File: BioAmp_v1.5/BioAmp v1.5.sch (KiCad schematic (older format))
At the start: 27 parts, among them J1 Conn_01x02_Male, J2 PJ-3062-CO, J4 Conn_01x03_Male, J5 Conn_01x02_Male, J6 Conn_01x02_Male, J7 Conn_01x02_Male, U1 TL074

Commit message: update v1.5.4
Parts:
- removed C2: 100nf, Capacitor_THT:C_Disc_D3.8mm_W2.6mm_P2.50mm, symbol Device:C
- added C2, C8: CP, Capacitor_THT:CP_Radial_D5.0mm_P2.50mm, symbol Device:CP
- S1: footprint udlabs:TL2285EE -> udlabs:G64_DPDT
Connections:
- net ACout: now also C2.2; no longer J2.2 (TIP), J2.3 (RING)
- net Aout: now also C2.1, C8.1
- new net ACout_spkr: C8.2, J2.2 (TIP), J2.3 (RING)
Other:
- moved on the sheet: J1, J2, J6
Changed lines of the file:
@@
 	1    0    0    -1
 $EndComp
-Text GLabel 3200 6350 2    50   Input ~ 0
+Text GLabel 3150 6350 2    50   Input ~ 0
 Vref
-Text GLabel 3200 6250 2    50   Input ~ 0
+Text GLabel 3150 6250 2    50   Input ~ 0
 Aout
-$Comp
-L Device:C C2
-U 1 1 5FD9D19F
-P 5250 5700
-F 0 "C2" H 5365 5746 50  0000 L CNN
-F 1 "100nf" H 5365 5655 50  0000 L CNN
-F 2 "Capacitor_THT:C_Disc_D3.8mm_W2.6mm_P2.50mm" H 5288 5550 50  0001 C CNN
-F 3 "~" H 5250 5700 50  0001 C CNN
-	1    5250 5700
-	1    0    0    -1
-$EndComp
 $Comp
 L Connector:Conn_01x02_Male J6
 U 1 1 5FD860E1
-P 3000 6250
-F 0 "J6" H 2900 6200 50  0000 C CNN
-F 1 "Conn_01x02_Male" H 2900 6350 50  0000 C CNN
-F 2 "Connector_PinHeader_2.54mm:PinHeader_1x02_P2.54mm_Vertical" H 3000 6250 50  0001 C CNN
-F 3 "~" H 3000 6250 50  0001 C CNN
-	1    3000 6250
-	1    0    0    -1
-$EndComp
-Text GLabel 5250 5850 3    50   Input ~ 0
+P 2950 6250
+F 0 "J6" H 2850 6200 50  0000 C CNN
+F 1 "Conn_01x02_Male" H 2850 6350 50  0000 C CNN
+F 2 "Connector_PinHeader_2.54mm:PinHeader_1x02_P2.54mm_Vertical" H 2950 6250 50  0001 C CNN
+F 3 "~" H 2950 6250 50  0001 C CNN
+	1    2950 6250
+	1    0    0    -1
+$EndComp
+Text GLabel 5150 5800 3    50   Input ~ 0
 Aout
-Text GLabel 5250 5550 1    50   Input ~ 0
+Text GLabel 5150 5500 1    50   Input ~ 0
 ACout
 $Comp
@@
 L Connector:Conn_01x02_Male J1
 U 1 1 5FE44E06
-P 4350 6050
-F 0 "J1" H 4250 6000 50  0000 C CNN
-F 1 "Conn_01x02_Male" H 4250 6150 50  0000 C CNN
-F 2 "Connector_PinHeader_2.54mm:PinHeader_1x02_P2.54mm_Vertical" H 4350 6050 50  0001 C CNN
-F 3 "~" H 4350 6050 50  0001 C CNN
-	1    4350 6050
-	1    0    0    -1
-$EndComp
-Text GLabel 4550 6150 2    50   Input ~ 0
+P 4300 6050
+F 0 "J1" H 4200 6000 50  0000 C CNN
+F 1 "Conn_01x02_Male" H 4200 6150 50  0000 C CNN
+F 2 "Connector_PinHeader_2.54mm:PinHeader_1x02_P2.54mm_Vertical" H 4300 6050 50  0001 C CNN
+F 3 "~" H 4300 6050 50  0001 C CNN
+	1    4300 6050
+	1    0    0    -1
+$EndComp
+Text GLabel 4500 6150 2    50   Input ~ 0
 Vref
 Wire Notes Line
@@
 Wire Notes Line
 	2450 6650 5650 6650
-Wire Notes Line
-	5650 6650 5650 4050
 Wire Notes Line
 	5650 4050 2450 4050
@@
 L udlabs:PJ-3062-CO J2
 U 1 1 6000E706
-P 2750 5500
-F 0 "J2" H 3550 6015 50  0000 C CNN
-F 1 "PJ-3062-CO" H 3550 5924 50  0000 C CNN
-F 2 "udlabs:PJ3062CO" H 4200 5850 50  0001 L CNN
-F 3 "https://datasheet.lcsc.com/szlcsc/1904121407_XKB-Enterprise-PJ-3062-CO_C319113.pdf" H 4200 5750 50  0001 L CNN
-F 4 "Audio & Video Connectors Female DIP RoHS" H 4200 5650 50  0001 L CNN "Description"
-F 5 "11" H 4200 5550 50  0001 L CNN "Height"
-F 6 "XKB Enterprise" H 4200 5450 50  0001 L CNN "Manufacturer_Name"
-F 7 "PJ-3062-CO" H 4200 5350 50  0001 L CNN "Manufacturer_Part_Number"
-	1    2750 5500
-	1    0    0    -1
-$EndComp
-Text GLabel 2750 5250 0    50   Input ~ 0
+P 2700 5500
+F 0 "J2" H 3500 6015 50  0000 C CNN
+F 1 "PJ-3062-CO" H 3500 5924 50  0000 C CNN
+F 2 "udlabs:PJ3062CO" H 4150 5850 50  0001 L CNN
+F 3 "https://datasheet.lcsc.com/szlcsc/1904121407_XKB-Enterprise-PJ-3062-CO_C319113.pdf" H 4150 5750 50  0001 L CNN
+F 4 "Audio & Video Connectors Female DIP RoHS" H 4150 5650 50  0001 L CNN "Description"
+F 5 "11" H 4150 5550 50  0001 L CNN "Height"
+F 6 "XKB Enterprise" H 4150 5450 50  0001 L CNN "Manufacturer_Name"
+F 7 "PJ-3062-CO" H 4150 5350 50  0001 L CNN "Manufacturer_Part_Number"
+	1    2700 5500
+	1    0    0    -1
+$EndComp
+Text GLabel 2700 5250 0    50   Input ~ 0
 Vref
-Text GLabel 4350 5550 2    50   Input ~ 0
-ACout
-Text GLabel 4350 5250 2    50   Input ~ 0
-ACout
+Text GLabel 4300 5550 2    50   Input ~ 0
+ACout_spkr
+Text GLabel 4300 5250 2    50   Input ~ 0
+ACout_spkr
 $Comp
 L Connector:Conn_01x03_Male J4
@@
 Vref
 Wire Wire Line
-	4350 5350 4350 5450
-Wire Wire Line
-	4350 5350 4750 5350
-Wire Wire Line
-	4750 5350 4750 6050
-Wire Wire Line
-	4550 6050 4750 6050
-Connection ~ 4350 5350
+	4300 5350 4300 5450
 $Comp
 L udlabs:TL2285EE S1
@@
 F 0 "S1" H 9050 3515 50  0000 C CNN
 F 1 "TL2285EE" H 9050 3424 50  0000 C CNN
-F 2 "udlabs:TL2285EE" H 9550 3350 50  0001 L CNN
+F 2 "udlabs:G64_DPDT" H 9550 3350 50  0001 L CNN
 F 3 "https://componentsearchengine.com/Datasheets/1/TL2285EE.pdf" H 9550 3250 50  0001 L CNN
 F 4 "Tactile Switches DPDT ALT ACT PC MNT" H 9550 3150 50  0001 L CNN "Description"
@@
 Wire Wire Line
 	7950 3550 7950 3450
+$Comp
+L Device:CP C2
+U 1 1 5FB85B2C
+P 5150 5650
+F 0 "C2" H 5268 5696 50  0000 L CNN
+F 1 "CP" H 5268 5605 50  0000 L CNN
+F 2 "Capacitor_THT:CP_Radial_D5.0mm_P2.50mm" H 5188 5500 50  0001 C CNN
+F 3 "~" H 5150 5650 50  0001 C CNN
+	1    5150 5650
+	-1   0    0    1
+$EndComp
+Wire Wire Line
+	4300 5350 4850 5350
+Wire Wire Line
+	4850 6050 4500 6050
+Connection ~ 4300 5350
+Wire Wire Line
+	4850 5350 4850 6050
+Text GLabel 5500 5500 1    50   Input ~ 0
+ACout_spkr
+Text GLabel 5500 5800 3    50   Input ~ 0
+Aout
+$Comp
+L Device:CP C8
+U 1 1 5FB8EAA6
+P 5500 5650
+F 0 "C8" H 5618 5696 50  0000 L CNN
+F 1 "CP" H 5618 5605 50  0000 L CNN
+F 2 "Capacitor_THT:CP_Radial_D5.0mm_P2.50mm" H 5538 5500 50  0001 C CNN
+F 3 "~" H 5500 5650 50  0001 C CNN
+	1    5500 5650
+	-1   0    0    1
+$EndComp
+Wire Notes Line
+	5650 6650 5650 4050
 $EndSCHEMATC

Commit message: Update to v1.5.5
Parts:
- removed S1: TL2285EE, udlabs:G64_DPDT, symbol udlabs:TL2285EE
- added SW1: G64_DPDT_7x7x12mm, udlabs:G64_DPDT_7x7x12mm, symbol udlabs:G64_DPDT_7x7x12mm
- C1, C3: value 100nf -> 4.7nf
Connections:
- net +9V: now also SW1.3 (B1)
- net B+: now also SW1.2 (C1)
- net B-: now also SW1.5 (C2)
- net GND: now also SW1.6 (B2)
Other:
- moved on the sheet: C1, C2, C3, C4, C5, C6, C7, C8, D1, J1, J2, J4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

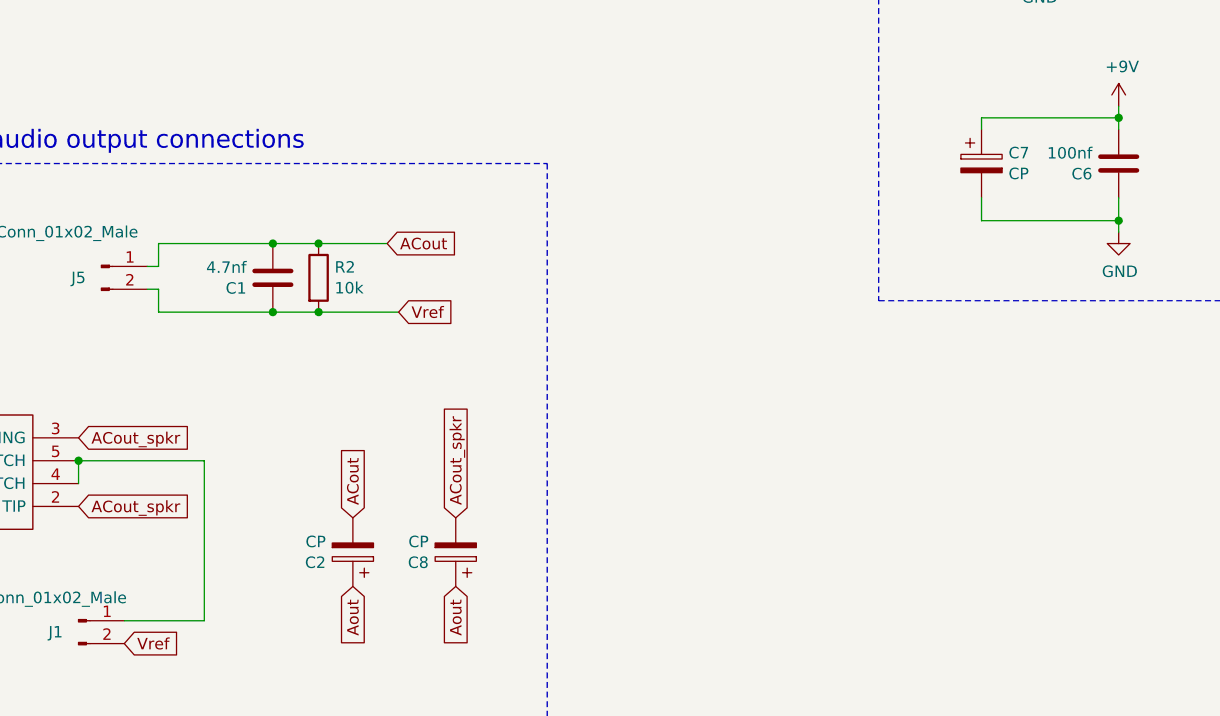
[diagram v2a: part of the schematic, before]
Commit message: Update schematic
Updated the capacitor referneces
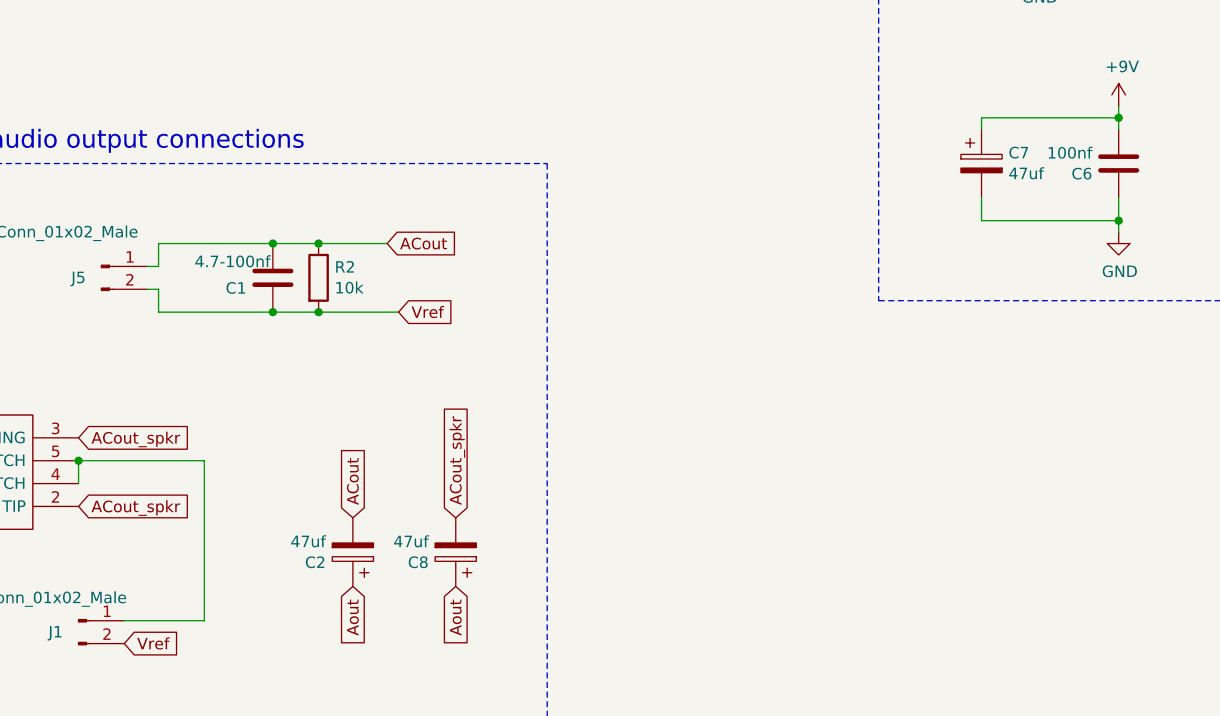
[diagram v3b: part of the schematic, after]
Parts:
- C1: value 4.7nf -> 4.7-100nf
- C2, C7, C8: value CP -> 47uf
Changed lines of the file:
@@
 P 7450 4400
 F 0 "C7" H 7568 4446 50  0000 L CNN
-F 1 "CP" H 7568 4355 50  0000 L CNN
+F 1 "47uf" H 7568 4355 50  0000 L CNN
 F 2 "Capacitor_THT:CP_Radial_D5.0mm_P2.50mm" H 7488 4250 50  0001 C CNN
 F 3 "~" H 7450 4400 50  0001 C CNN
@@
 P 5150 6100
 F 0 "C8" H 5268 6146 50  0000 L CNN
-F 1 "CP" H 5268 6055 50  0000 L CNN
+F 1 "47uf" H 5268 6055 50  0000 L CNN
 F 2 "Capacitor_THT:CP_Radial_D5.0mm_P2.50mm" H 5188 5950 50  0001 C CNN
 F 3 "~" H 5150 6100 50  0001 C CNN
@@
 P 4700 6100
 F 0 "C2" H 4818 6146 50  0000 L CNN
-F 1 "CP" H 4818 6055 50  0000 L CNN
+F 1 "47uf" H 4818 6055 50  0000 L CNN
 F 2 "Capacitor_THT:CP_Radial_D5.0mm_P2.50mm" H 4738 5950 50  0001 C CNN
 F 3 "~" H 4700 6100 50  0001 C CNN
@@
 P 4350 4900
 F 0 "C1" H 4465 4946 50  0000 L CNN
-F 1 "4.7nf" H 4465 4855 50  0000 L CNN
+F 1 "4.7-100nf" H 4360 4830 50  0000 L CNN
 F 2 "Capacitor_THT:C_Disc_D3.8mm_W2.6mm_P2.50mm" H 4388 4750 50  0001 C CNN
 F 3 "~" H 4350 4900 50  0001 C CNN
